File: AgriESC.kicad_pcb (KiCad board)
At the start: 2 copper layers, 94.5 x 53.5 mm, 309 parts, among them J1 SUPPLY, J10 GPIO, J11 USB_OTG, J12 HALL_ENC, J2 PH_A, J3 PH_B, J4 PH_C, J6 COMM, J7 SERVO, J8 CAN, J9 SWD, SW1 SW_SPDT, U1 FDMS7698, U10 STM32F405RGT6, U11 DRV8303, U12 TJA1051TK-3, U13 LMR16006YQ, U14 MCP1700-3302E_SOT23, U15 MCP1700-3302E_SOT23, U2 FDMS7698, U3 FDMS7698, U4 FDMS7698, U5 FDMS7698, U6 FDMS7698, U7 MAX9920, U8 MAX9920, U9 MAX9920, Y1 8M Resonator

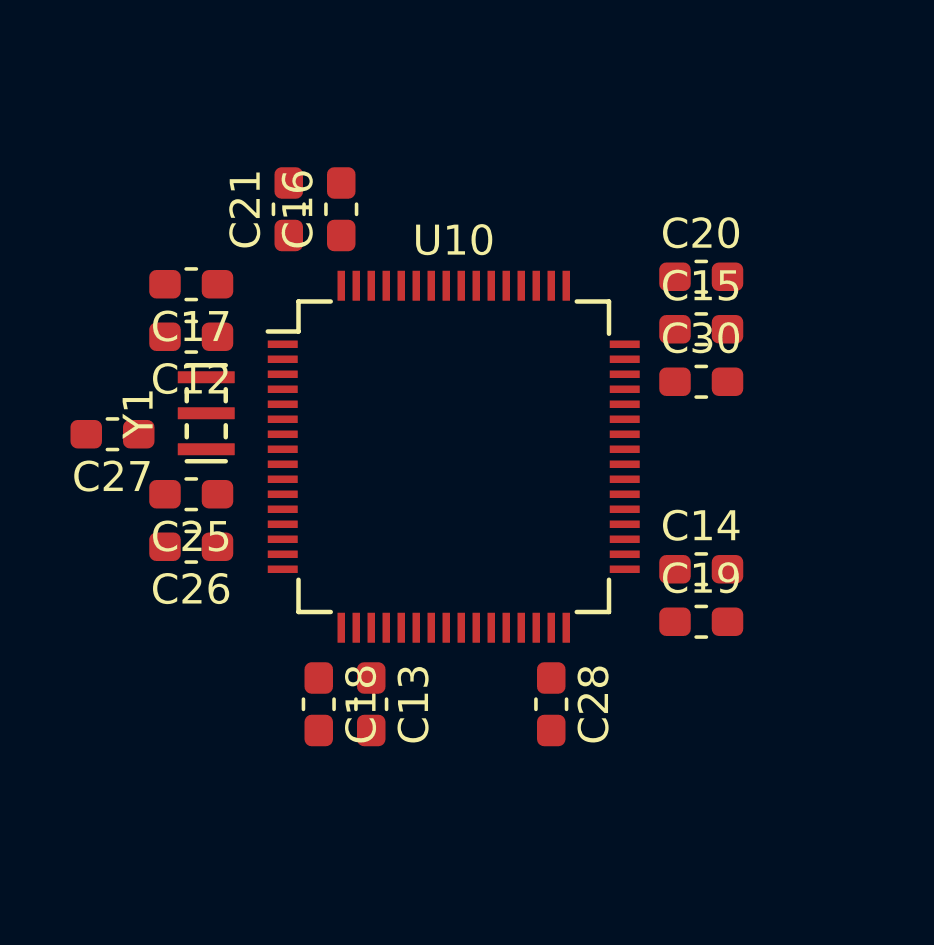
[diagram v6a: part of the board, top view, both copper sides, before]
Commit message: Wiring for microprocessor
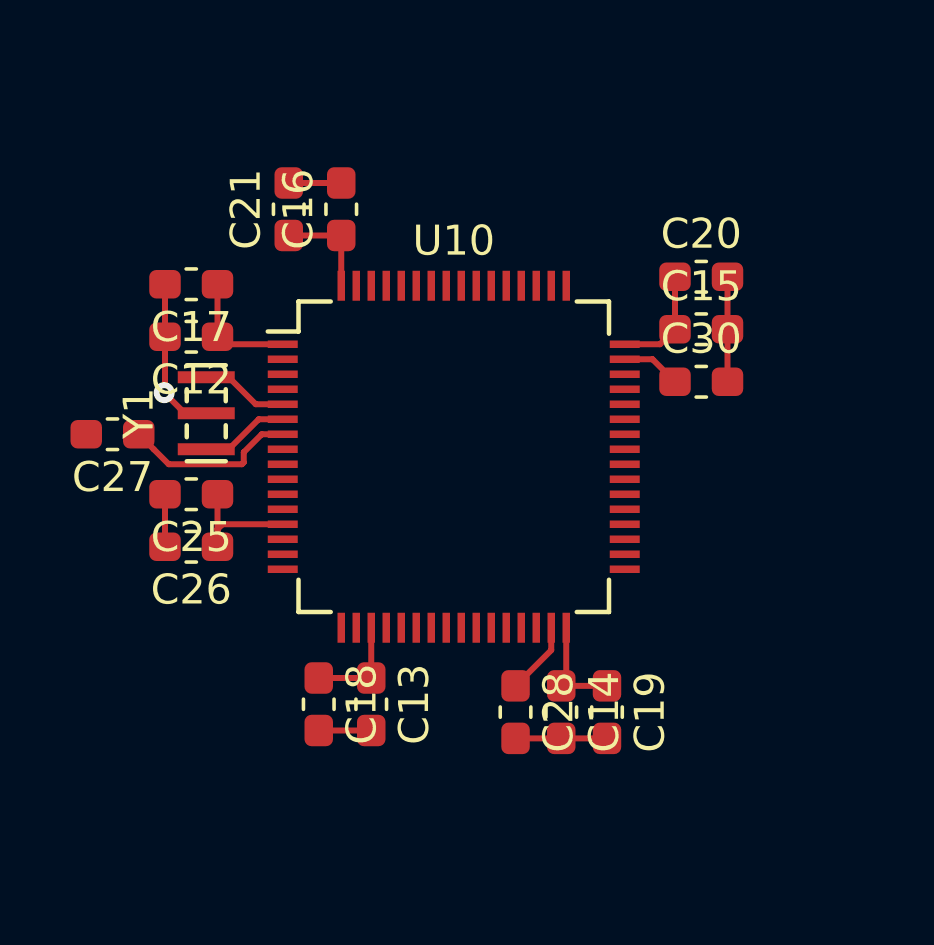
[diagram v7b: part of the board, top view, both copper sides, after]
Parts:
- moved C14 6.67 mm to (-26.4, 32.5), turned to 270 degrees
- moved C19 4.35 mm to (-24.9, 32.5), turned to 270 degrees
- moved C28 1.22 mm to (-27.9, 32.5)
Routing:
- net VCC: track 14.8 -> 32.8 mm
- net SL_A: track 290.5 -> 307.6 mm, vias 15 -> 16
- net NRST: track 0.00 -> 5.83 mm
- net VAA: track 89.3 -> 93.3 mm
- net Net-(U10-Pad6): track 0.00 -> 2.96 mm
- net Net-(U10-Pad5): track 0.00 -> 2.92 mm
- net Net-(C28-Pad1): track 0.00 -> 2.43 mm
- net Net-(C30-Pad1): track 0.00 -> 1.99 mm
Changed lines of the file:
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@@
     (thickness 1.6)
     (drawings 4)
-    (tracks 593)
+    (tracks 640)
     (zones 0)
     (modules 309)
@@
   )
   (module Capacitor_SMD:C_0603_1608Metric_Pad1.05x0.95mm_HandSolder (layer F.Cu)
-    (at -21.75 27.75)
+    (at -26.416 32.512 270)
     (descr "Capacitor SMD 0603 (1608 Metric), square (rectangular) end terminal, IPC_7351 nominal with elongated pad for handsoldering. (Body size source: http://www.tortai-tech.com/upload/download/2011102023233369053.pdf), generated with kicad-footprint-generator")
     (tags "capacitor handsolder")
     (attr smd)
-    (fp_text reference C14 (at 0 -1.43) (layer F.SilkS)
+    (fp_text reference C14 (at 0 -1.43 270) (layer F.SilkS)
       (effects (font (size 1 1) (thickness 0.15)))
     )
-    (fp_text value 100n (at 0 1.43) (layer F.Fab)
+    (fp_text value 100n (at 0 1.43 270) (layer F.Fab)
       (effects (font (size 1 1) (thickness 0.15)))
     )
@@
     (fp_line (start 1.65 -0.73) (end 1.65 0.73) (layer F.CrtYd) (width 0.05))
     (fp_line (start 1.65 0.73) (end -1.65 0.73) (layer F.CrtYd) (width 0.05))
-    (fp_text user %R (at 0 0) (layer F.Fab)
+    (fp_text user %R (at 0 0 270) (layer F.Fab)
       (effects (font (size 0.4 0.4) (thickness 0.06)))
     )
-    (pad 1 smd roundrect (at -0.875 0) (size 1.05 0.95) (layers F.Cu F.Paste F.Mask) (roundrect_rratio 0.25)
+    (pad 1 smd roundrect (at -0.875 0 270) (size 1.05 0.95) (layers F.Cu F.Paste F.Mask) (roundrect_rratio 0.25)
       (net 4 VCC))
-    (pad 2 smd roundrect (at 0.875 0) (size 1.05 0.95) (layers F.Cu F.Paste F.Mask) (roundrect_rratio 0.25)
+    (pad 2 smd roundrect (at 0.875 0 270) (size 1.05 0.95) (layers F.Cu F.Paste F.Mask) (roundrect_rratio 0.25)
       (net 1 SL_A))
     (model ${KISYS3DMOD}/Capacitor_SMD.3dshapes/C_0603_1608Metric.wrl
@@
   )
   (module Capacitor_SMD:C_0603_1608Metric_Pad1.05x0.95mm_HandSolder (layer F.Cu)
-    (at -21.75 29.5)
+    (at -24.892 32.512 270)
     (descr "Capacitor SMD 0603 (1608 Metric), square (rectangular) end terminal, IPC_7351 nominal with elongated pad for handsoldering. (Body size source: http://www.tortai-tech.com/upload/download/2011102023233369053.pdf), generated with kicad-footprint-generator")
     (tags "capacitor handsolder")
     (attr smd)
-    (fp_text reference C19 (at 0 -1.43) (layer F.SilkS)
+    (fp_text reference C19 (at 0 -1.43 270) (layer F.SilkS)
       (effects (font (size 1 1) (thickness 0.15)))
     )
-    (fp_text value 2u2 (at 0 1.43) (layer F.Fab)
+    (fp_text value 2u2 (at 0 1.43 270) (layer F.Fab)
       (effects (font (size 1 1) (thickness 0.15)))
     )
@@
     (fp_line (start 1.65 -0.73) (end 1.65 0.73) (layer F.CrtYd) (width 0.05))
     (fp_line (start 1.65 0.73) (end -1.65 0.73) (layer F.CrtYd) (width 0.05))
-    (fp_text user %R (at 0 0) (layer F.Fab)
+    (fp_text user %R (at 0 0 270) (layer F.Fab)
       (effects (font (size 0.4 0.4) (thickness 0.06)))
     )
-    (pad 1 smd roundrect (at -0.875 0) (size 1.05 0.95) (layers F.Cu F.Paste F.Mask) (roundrect_rratio 0.25)
+    (pad 1 smd roundrect (at -0.875 0 270) (size 1.05 0.95) (layers F.Cu F.Paste F.Mask) (roundrect_rratio 0.25)
       (net 4 VCC))
-    (pad 2 smd roundrect (at 0.875 0) (size 1.05 0.95) (layers F.Cu F.Paste F.Mask) (roundrect_rratio 0.25)
+    (pad 2 smd roundrect (at 0.875 0 270) (size 1.05 0.95) (layers F.Cu F.Paste F.Mask) (roundrect_rratio 0.25)
       (net 1 SL_A))
     (model ${KISYS3DMOD}/Capacitor_SMD.3dshapes/C_0603_1608Metric.wrl
@@
   )
   (module Capacitor_SMD:C_0603_1608Metric_Pad1.05x0.95mm_HandSolder (layer F.Cu)
-    (at -26.75 32.25 270)
+    (at -27.94 32.512 270)
     (descr "Capacitor SMD 0603 (1608 Metric), square (rectangular) end terminal, IPC_7351 nominal with elongated pad for handsoldering. (Body size source: http://www.tortai-tech.com/upload/download/2011102023233369053.pdf), generated with kicad-footprint-generator")
     (tags "capacitor handsolder")
@@
   (segment (start -11.01 -15.914) (end -10.16 -16.764) (width 0.2) (layer F.Cu) (net 1))
   (segment (start -11.01 -15.748) (end -11.01 -15.914) (width 0.2) (layer F.Cu) (net 1))
+  (segment (start -39.625 20) (end -39.625 18.25) (width 0.2) (layer F.Cu) (net 1))
+  (segment (start -33.75 14.875) (end -35.5 14.875) (width 0.2) (layer F.Cu) (net 1))
+  (segment (start -39.625 25.25) (end -39.625 27) (width 0.2) (layer F.Cu) (net 1))
+  (segment (start -38.965376 22.55) (end -39.651977 21.863399) (width 0.2) (layer F.Cu) (net 1))
+  (segment (start -38.25 22.55) (end -38.965376 22.55) (width 0.2) (layer F.Cu) (net 1))
+  (segment (start -39.625 21.836422) (end -39.651977 21.863399) (width 0.2) (layer F.Cu) (net 1))
+  (segment (start -39.625 20) (end -39.625 21.836422) (width 0.2) (layer F.Cu) (net 1))
+  (via (at -39.651977 21.863399) (size 0.7) (drill 0.3) (layers F.Cu B.Cu) (net 1))
+  (segment (start -20.875 18) (end -20.875 19.75) (width 0.2) (layer F.Cu) (net 1))
+  (segment (start -20.875 21.5) (end -20.875 19.75) (width 0.2) (layer F.Cu) (net 1))
+  (segment (start -27.94 33.387) (end -26.416 33.387) (width 0.2) (layer F.Cu) (net 1))
+  (segment (start -26.416 33.387) (end -24.892 33.387) (width 0.2) (layer F.Cu) (net 1))
+  (segment (start -32.75 33.125) (end -34.5 33.125) (width 0.2) (layer F.Cu) (net 1))
   (segment (start 114.775 22.975) (end 114.75 23) (width 0.25) (layer F.Cu) (net 2))
   (segment (start 114.775 21) (end 114.775 22.975) (width 0.25) (layer F.Cu) (net 2))
@@
   (segment (start 42.105 -11.825) (end 42.18 -11.75) (width 0.4) (layer F.Cu) (net 3))
   (segment (start 40.005 -11.825) (end 42.105 -11.825) (width 0.4) (layer F.Cu) (net 3))
+  (segment (start -37.709 26.25) (end -37.875 26.416) (width 0.2) (layer F.Cu) (net 3))
+  (segment (start -35.7 26.25) (end -37.709 26.25) (width 0.2) (layer F.Cu) (net 3))
+  (segment (start -37.875 26.416) (end -37.875 27) (width 0.2) (layer F.Cu) (net 3))
+  (segment (start -37.875 25.25) (end -37.875 26.416) (width 0.2) (layer F.Cu) (net 3))
   (segment (start 58.615 -8.015) (end 58.69 -7.94) (width 0.4) (layer F.Cu) (net 4))
   (segment (start 56.515 -8.015) (end 58.615 -8.015) (width 0.4) (layer F.Cu) (net 4))
@@
   (segment (start 1.889844 -16.75) (end 3.935844 -18.796) (width 0.2) (layer F.Cu) (net 4))
   (segment (start 3.935844 -18.796) (end 7.112 -18.796) (width 0.2) (layer F.Cu) (net 4))
+  (segment (start -37.625 20.25) (end -37.875 20) (width 0.2) (layer F.Cu) (net 4))
+  (segment (start -35.7 20.25) (end -37.625 20.25) (width 0.2) (layer F.Cu) (net 4))
+  (segment (start -37.875 20) (end -37.875 18.25) (width 0.2) (layer F.Cu) (net 4))
+  (segment (start -35.5 16.625) (end -33.75 16.625) (width 0.2) (layer F.Cu) (net 4))
+  (segment (start -33.75 18.3) (end -33.75 16.625) (width 0.2) (layer F.Cu) (net 4))
+  (segment (start -23.125 20.25) (end -22.625 19.75) (width 0.2) (layer F.Cu) (net 4))
+  (segment (start -24.3 20.25) (end -23.125 20.25) (width 0.2) (layer F.Cu) (net 4))
+  (segment (start -22.625 18) (end -22.625 19.75) (width 0.2) (layer F.Cu) (net 4))
+  (segment (start -24.892 31.637) (end -26.416 31.637) (width 0.2) (layer F.Cu) (net 4))
+  (segment (start -26.25 31.471) (end -26.416 31.637) (width 0.2) (layer F.Cu) (net 4))
+  (segment (start -26.25 29.7) (end -26.25 31.471) (width 0.2) (layer F.Cu) (net 4))
+  (segment (start -32.75 29.7) (end -32.75 31.375) (width 0.2) (layer F.Cu) (net 4))
+  (segment (start -32.75 31.375) (end -34.5 31.375) (width 0.2) (layer F.Cu) (net 4))
+  (segment (start -39.499999 24.250001) (end -40.000928 23.749072) (width 0.2) (layer F.Cu) (net 8))
+  (segment (start -36.999999 24.190001) (end -37.059999 24.250001) (width 0.2) (layer F.Cu) (net 8))
+  (segment (start -40.000928 23.749072) (end -40.5 23.25) (width 0.2) (layer F.Cu) (net 8))
+  (segment (start -36.999999 23.849999) (end -36.999999 24.190001) (width 0.2) (layer F.Cu) (net 8))
+  (segment (start -37.059999 24.250001) (end -39.499999 24.250001) (width 0.2) (layer F.Cu) (net 8))
+  (segment (start -36.4 23.25) (end -36.999999 23.849999) (width 0.2) (layer F.Cu) (net 8))
+  (segment (start -35.7 23.25) (end -36.4 23.25) (width 0.2) (layer F.Cu) (net 8))
+  (segment (start -26.75 30.447) (end -27.94 31.637) (width 0.2) (layer F.Cu) (net 9))
+  (segment (start -26.75 29.7) (end -26.75 30.447) (width 0.2) (layer F.Cu) (net 9))
+  (segment (start -23.375 20.75) (end -22.625 21.5) (width 0.2) (layer F.Cu) (net 11))
+  (segment (start -24.3 20.75) (end -23.375 20.75) (width 0.2) (layer F.Cu) (net 11))
   (segment (start 119.217 34.5) (end 119.25 34.5) (width 0.2) (layer F.Cu) (net 12))
   (segment (start 117.405 36.312) (end 119.217 34.5) (width 0.2) (layer F.Cu) (net 12))
@@
   (segment (start 54.295 86.53) (end 52.48 86.53) (width 0.2) (layer F.Cu) (net 86))
   (segment (start 52.31 86.36) (end 52.31 84.455) (width 0.2) (layer F.Cu) (net 86))
+  (segment (start -37.5 21.35) (end -38.25 21.35) (width 0.2) (layer F.Cu) (net 90))
+  (segment (start -36.6 22.25) (end -37.5 21.35) (width 0.2) (layer F.Cu) (net 90))
+  (segment (start -35.7 22.25) (end -36.6 22.25) (width 0.2) (layer F.Cu) (net 90))
+  (segment (start -37.5 23.75) (end -38.25 23.75) (width 0.2) (layer F.Cu) (net 91))
+  (segment (start -36.5 22.75) (end -37.5 23.75) (width 0.2) (layer F.Cu) (net 91))
+  (segment (start -35.7 22.75) (end -36.5 22.75) (width 0.2) (layer F.Cu) (net 91))
   (segment (start -6.5 -11.75) (end -15.555 -11.75) (width 0.2) (layer F.Cu) (net 93))
   (segment (start -6.5 -10.75) (end -14.56 -10.75) (width 0.2) (layer F.Cu) (net 94))

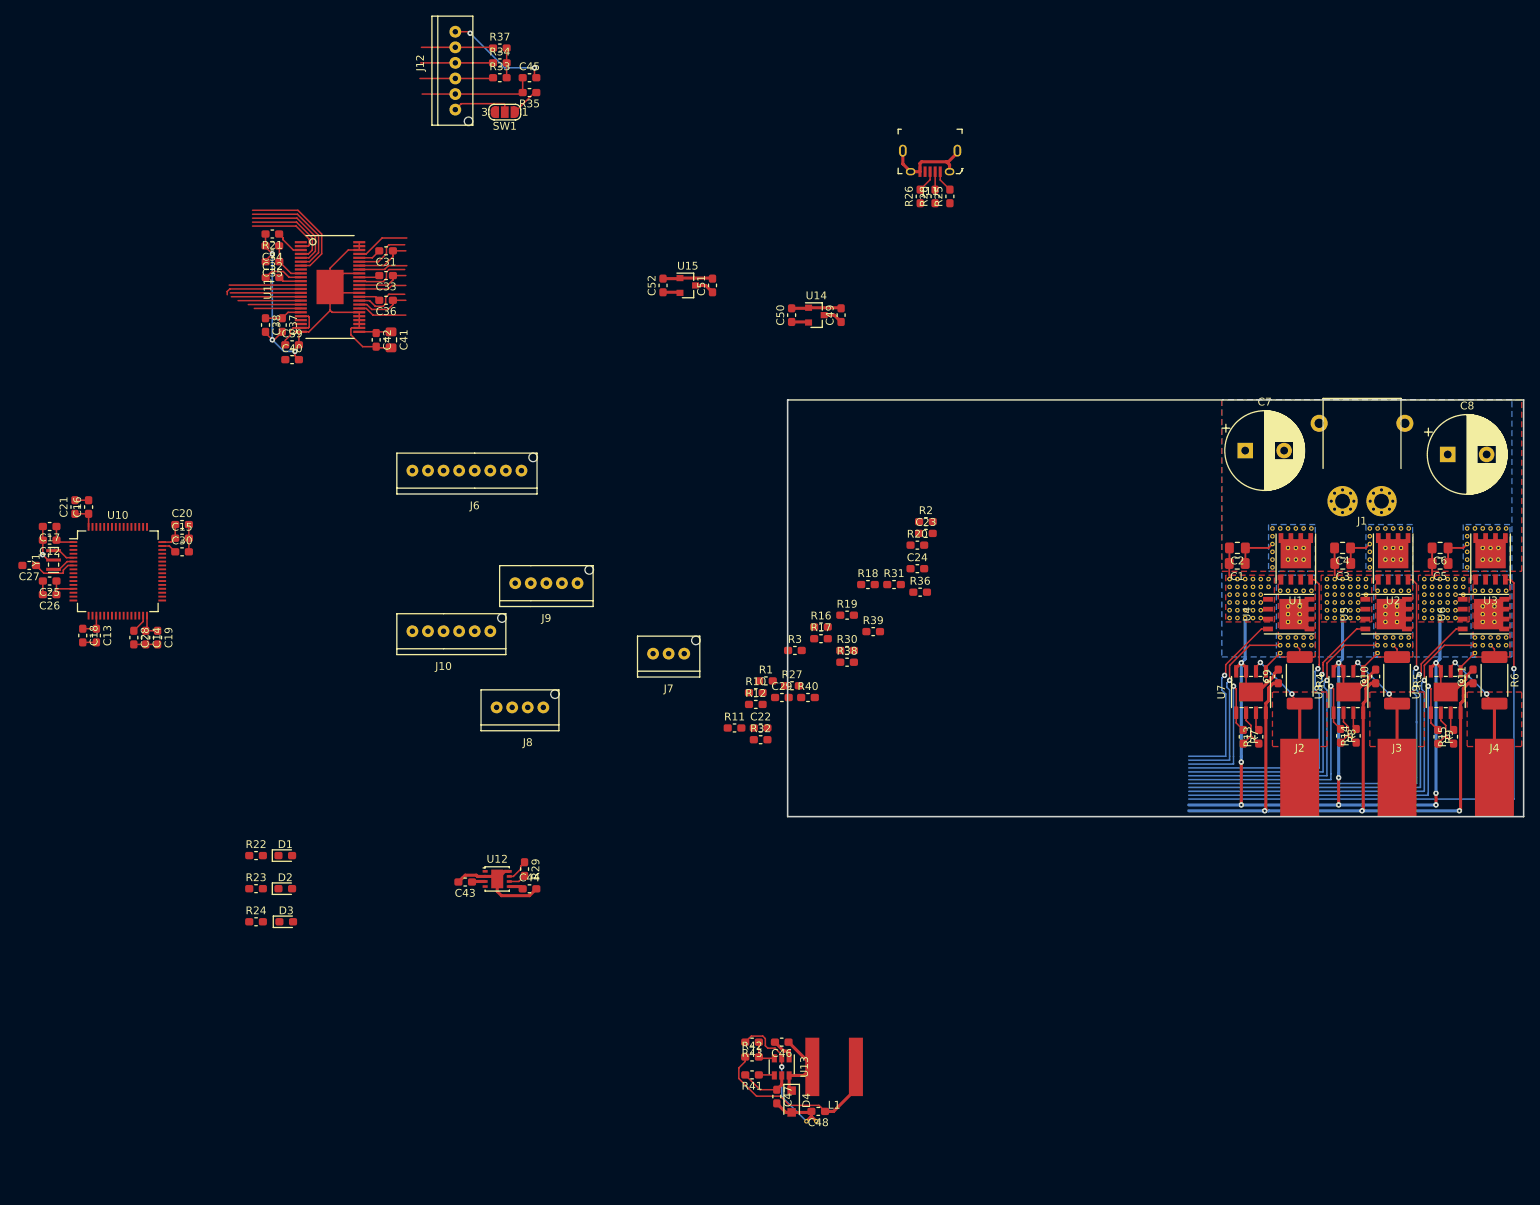
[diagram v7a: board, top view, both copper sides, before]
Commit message: Started arranging components
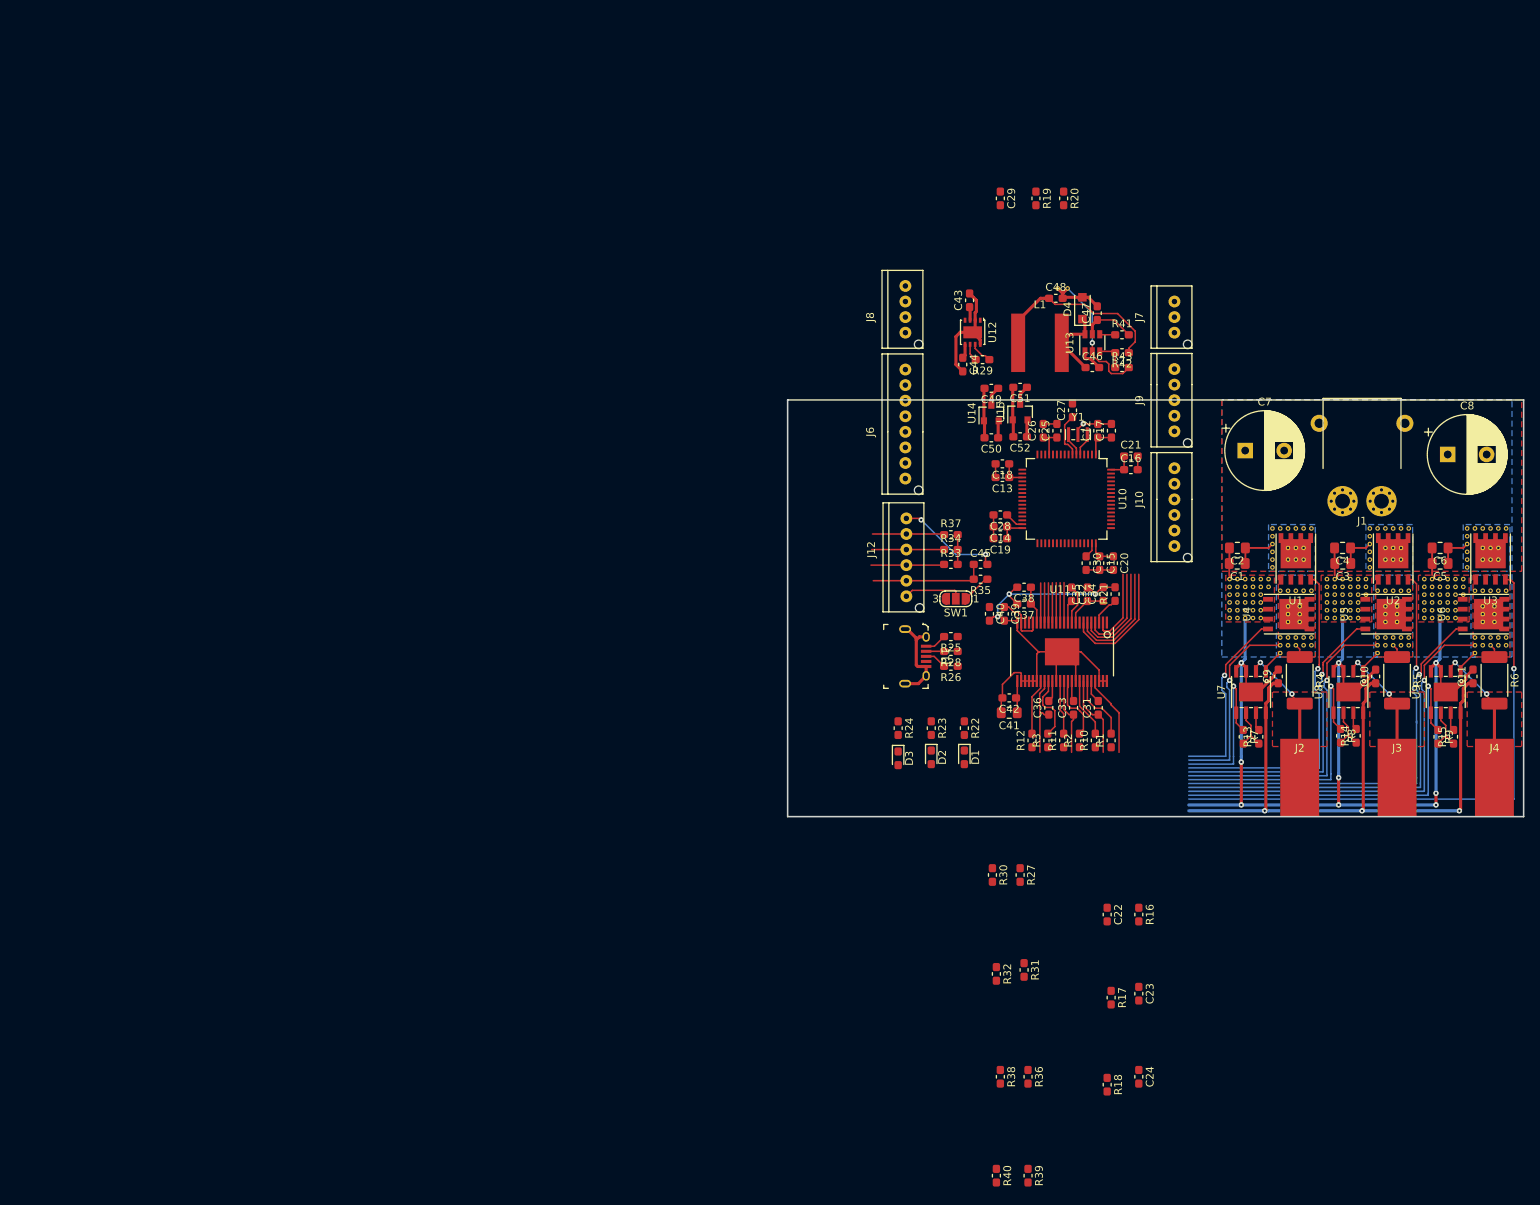
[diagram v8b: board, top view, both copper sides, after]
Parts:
- moved C17 136.9 mm to (97.6, 5.95), turned to 90 degrees
- moved C21 135.7 mm to (100.1, 9.20), turned to 0 degrees
- moved C27 135.4 mm to (92.6, 3.33), turned to 90 degrees
- moved C12 135.3 mm to (95.8, 5.95), turned to 90 degrees
- moved C16 133.9 mm to (100.1, 11.0), turned to 0 degrees
- moved Y1 132.5 mm to (93.3, 6.45), turned to 180 degrees
- moved C25 130.8 mm to (90.6, 5.95), turned to 90 degrees
- moved C26 129.3 mm to (88.8, 5.95), turned to 90 degrees
- moved U10 122.2 mm to (91.8, 14.7), turned to 270 degrees
- moved C18 120.1 mm to (83.6, 10.2), turned to 180 degrees
- moved C20 119.7 mm to (97.8, 23.0), turned to 270 degrees
- moved C13 118.1 mm to (83.6, 12.0), turned to 180 degrees
- moved C15 117.9 mm to (96.1, 23.0), turned to 270 degrees
- moved R21 117.7 mm to (98.0, 26.9), turned to 90 degrees
- moved C30 116.1 mm to (94.3, 23.0), turned to 270 degrees
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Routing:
- net H1: track 10.00 -> 5.13 mm
- net EN_GATE: track 9.20 -> 5.13 mm
- net INL_A: track 9.05 -> 5.12 mm
- net H2: track 8.92 -> 5.11 mm
- net SH_C: track 66.2 -> 69.8 mm
- net VCC: track 32.8 -> 36.3 mm
- net SH_A: track 37.3 -> 40.8 mm
- net SH_B: track 51.6 -> 54.9 mm
- net INL_B: track 8.06 -> 5.10 mm
- net H3: track 6.74 -> 5.09 mm
- net GH_B: track 6.99 -> 8.31 mm
- net GH_C: track 7.27 -> 8.56 mm
- net GL_A: track 6.31 -> 7.60 mm
- net GH_A: track 7.22 -> 8.50 mm
- net INL_C: track 5.97 -> 5.09 mm
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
